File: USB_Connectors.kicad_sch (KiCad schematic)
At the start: 109 parts, among them J1 USB_C_Receptacle, J2 USB_C_Receptacle, J3 USB_C_Receptacle_USB2.0_16P, Q1 60/100V, Q2 60/100V, Q3 60/100V, Q4 60/100V, Q5 2N7002K, Q6 2N7002K, Q7 60/100V, Q8 2N7002K, Q9 60/100V, U2 RAA489400, U3 RAA489400, U4 RAA489400

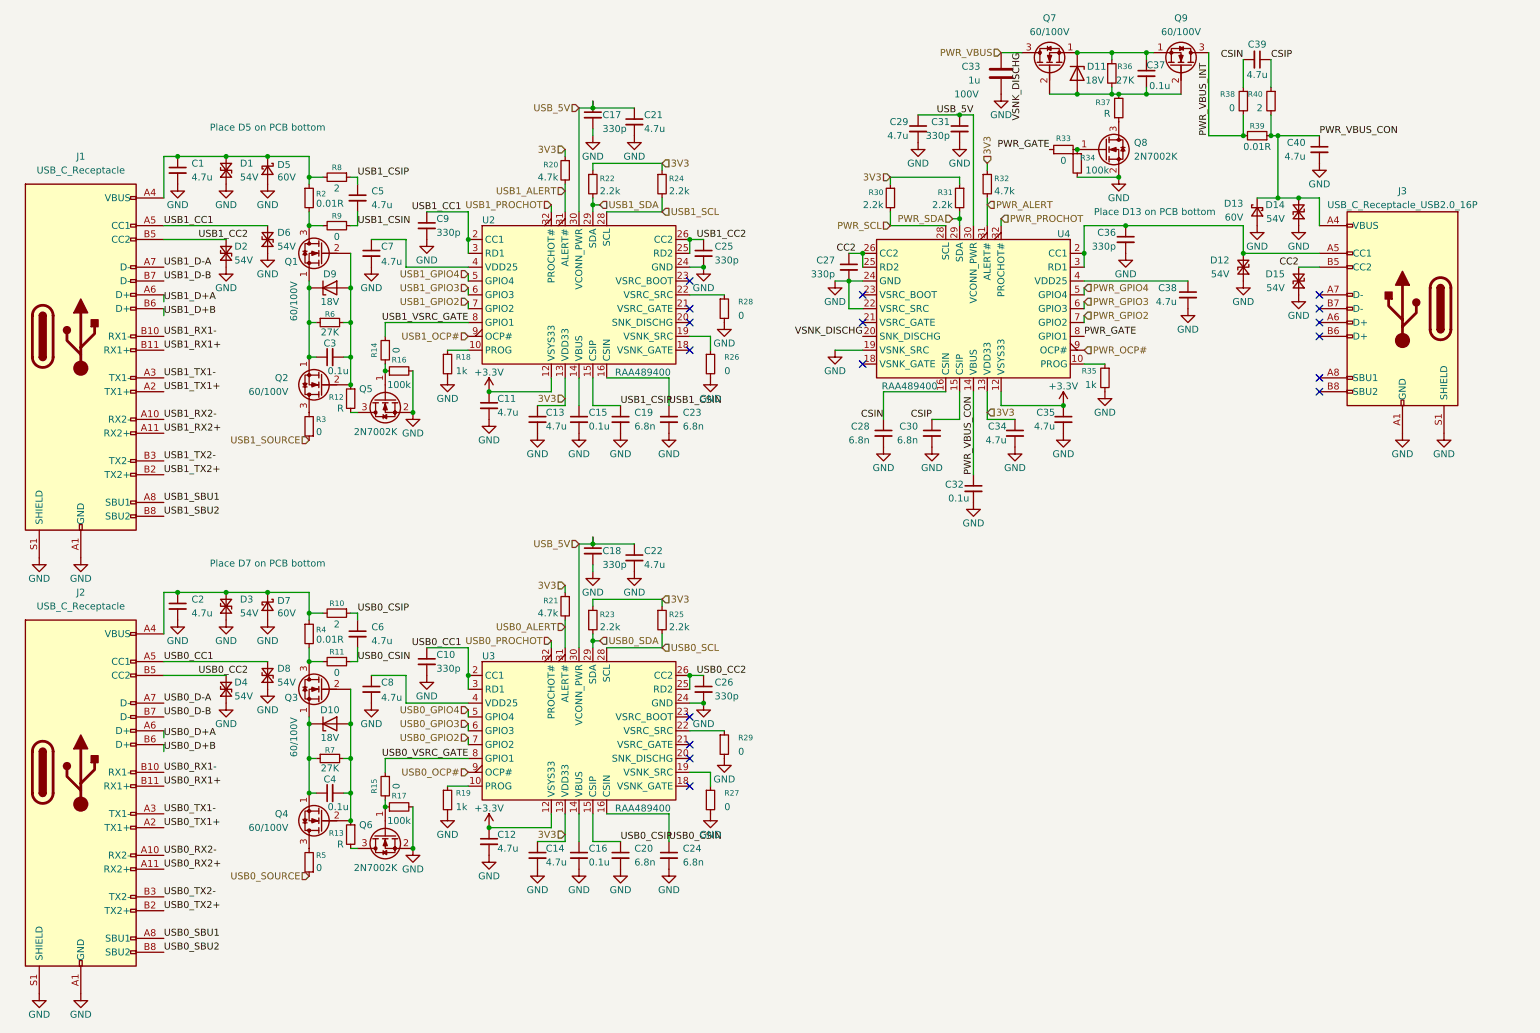
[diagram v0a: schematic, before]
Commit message: USB superspeed muxes
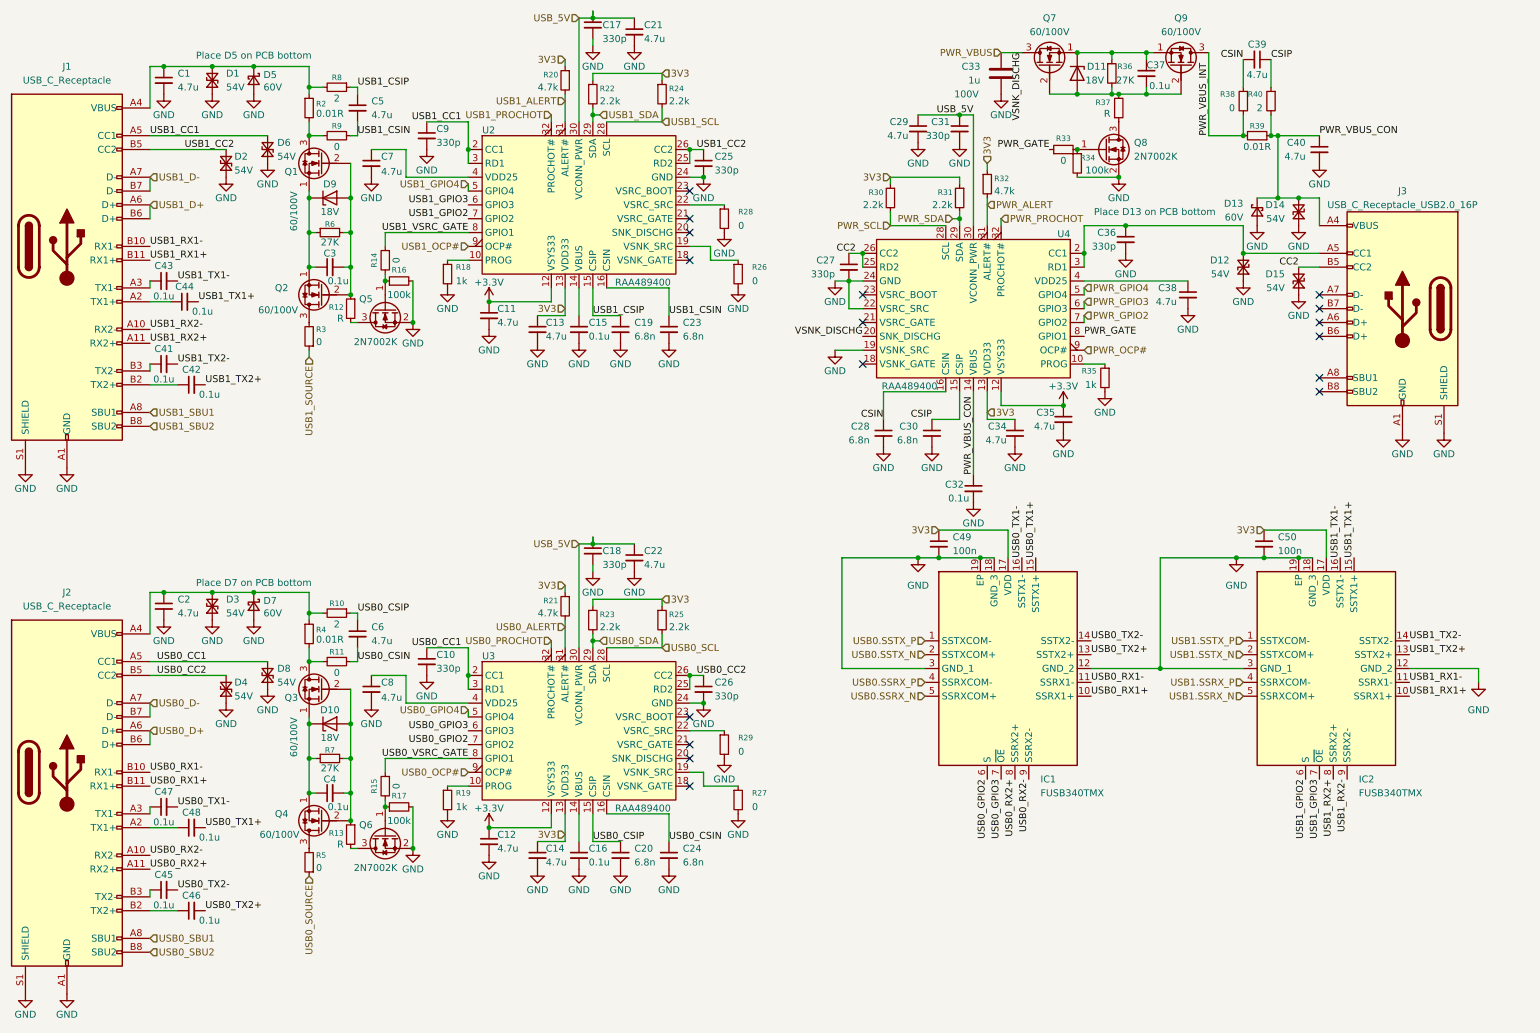
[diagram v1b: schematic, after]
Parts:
- added C41, C42, C43, C44, C45, C46, C47, C48: 0.1u, symbol Device:C_Small
- added C49, C50: 100n, symbol Device:C_Small
- added IC1, IC2: FUSB340TMX, onsemi:FUSB340TMX, symbol onsemi:FUSB340TMX
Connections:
- net USB0_D+B is gone; now on net USB0_D+: J2.B6 (D+)
- net USB0_D-B is gone; now on net USB0_D-: J2.B7 (D-)
- net USB1_D+B is gone; now on net USB1_D+: J1.B6 (D+)
- net USB1_D-B is gone; now on net USB1_D-: J1.B7 (D-)
- net 3V3: now also C49.1, C50.1, IC1.17 (VDD), IC2.17 (VDD)
- net GND: now also C49.2, C50.2, IC1.12 (GND_2), IC1.18 (GND_3), IC1.19 (EP), IC1.3 (GND_1), IC2.12 (GND_2), IC2.18 (GND_3), IC2.19 (EP), IC2.3 (GND_1)
- net USB0_GPIO2: now also IC1.6 (S)
- net USB0_GPIO3: now also IC1.7 (~{OE})
- net USB0_RX1+: now also IC1.10 (SSRX1+)
- net USB0_RX1-: now also IC1.11 (SSRX1-)
- net USB0_RX2+: now also IC1.8 (SSRX2+)
- net USB0_RX2-: now also IC1.9 (SSRX2-)
- net USB0_TX1+: now also C48.2, IC1.15 (SSTX1+); no longer J2.A2 (TX1+)
- net USB0_TX1-: now also C47.2, IC1.16 (SSTX1-); no longer J2.A3 (TX1-)
- net USB0_TX2+: now also C46.2, IC1.13 (SSTX2+); no longer J2.B2 (TX2+)
- net USB0_TX2-: now also C45.2, IC1.14 (SSTX2-); no longer J2.B3 (TX2-)
- net USB1_GPIO2: now also IC2.6 (S)
- net USB1_GPIO3: now also IC2.7 (~{OE})
- net USB1_RX1+: now also IC2.10 (SSRX1+)
- net USB1_RX1-: now also IC2.11 (SSRX1-)
- net USB1_RX2+: now also IC2.8 (SSRX2+)
- net USB1_RX2-: now also IC2.9 (SSRX2-)
- net USB1_TX1+: now also C44.2, IC2.15 (SSTX1+); no longer J1.A2 (TX1+)
- net USB1_TX1-: now also C43.2, IC2.16 (SSTX1-); no longer J1.A3 (TX1-)
- net USB1_TX2+: now also C42.2, IC2.13 (SSTX2+); no longer J1.B2 (TX2+)
- net USB1_TX2-: now also C41.2, IC2.14 (SSTX2-); no longer J1.B3 (TX2-)
- net USB0_D+A renamed USB0_D+
- net USB0_D-A renamed USB0_D-
- net USB1_D+A renamed USB1_D+
- net USB1_D-A renamed USB1_D-
- new net: C42.1, J1.B2 (TX2+)
- new net: C48.1, J2.A2 (TX1+)
- new net: C47.1, J2.A3 (TX1-)
- new net: C46.1, J2.B2 (TX2+)
- new net: C45.1, J2.B3 (TX2-)
- new net: C43.1, J1.A3 (TX1-)
- new net: C44.1, J1.A2 (TX1+)
- new net: C41.1, J1.B3 (TX2-)
- new net USB0.SSRX_N: IC1.5 (SSRXCOM+)
- new net USB0.SSRX_P: IC1.4 (SSRXCOM-)
- new net USB0.SSTX_N: IC1.2 (SSTXCOM+)
- new net USB0.SSTX_P: IC1.1 (SSTXCOM-)
- new net USB1.SSRX_N: IC2.5 (SSRXCOM+)
- new net USB1.SSRX_P: IC2.4 (SSRXCOM-)
- new net USB1.SSTX_N: IC2.2 (SSTXCOM+)
- new net USB1.SSTX_P: IC2.1 (SSTXCOM-)
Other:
- moved on the sheet: C1, C11, C13, C15, C17, C19, C2, C21, C23, C25, C3, C5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

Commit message: changed USB connectors added superspeed ESD updated USB-PD I2C PROG resistors
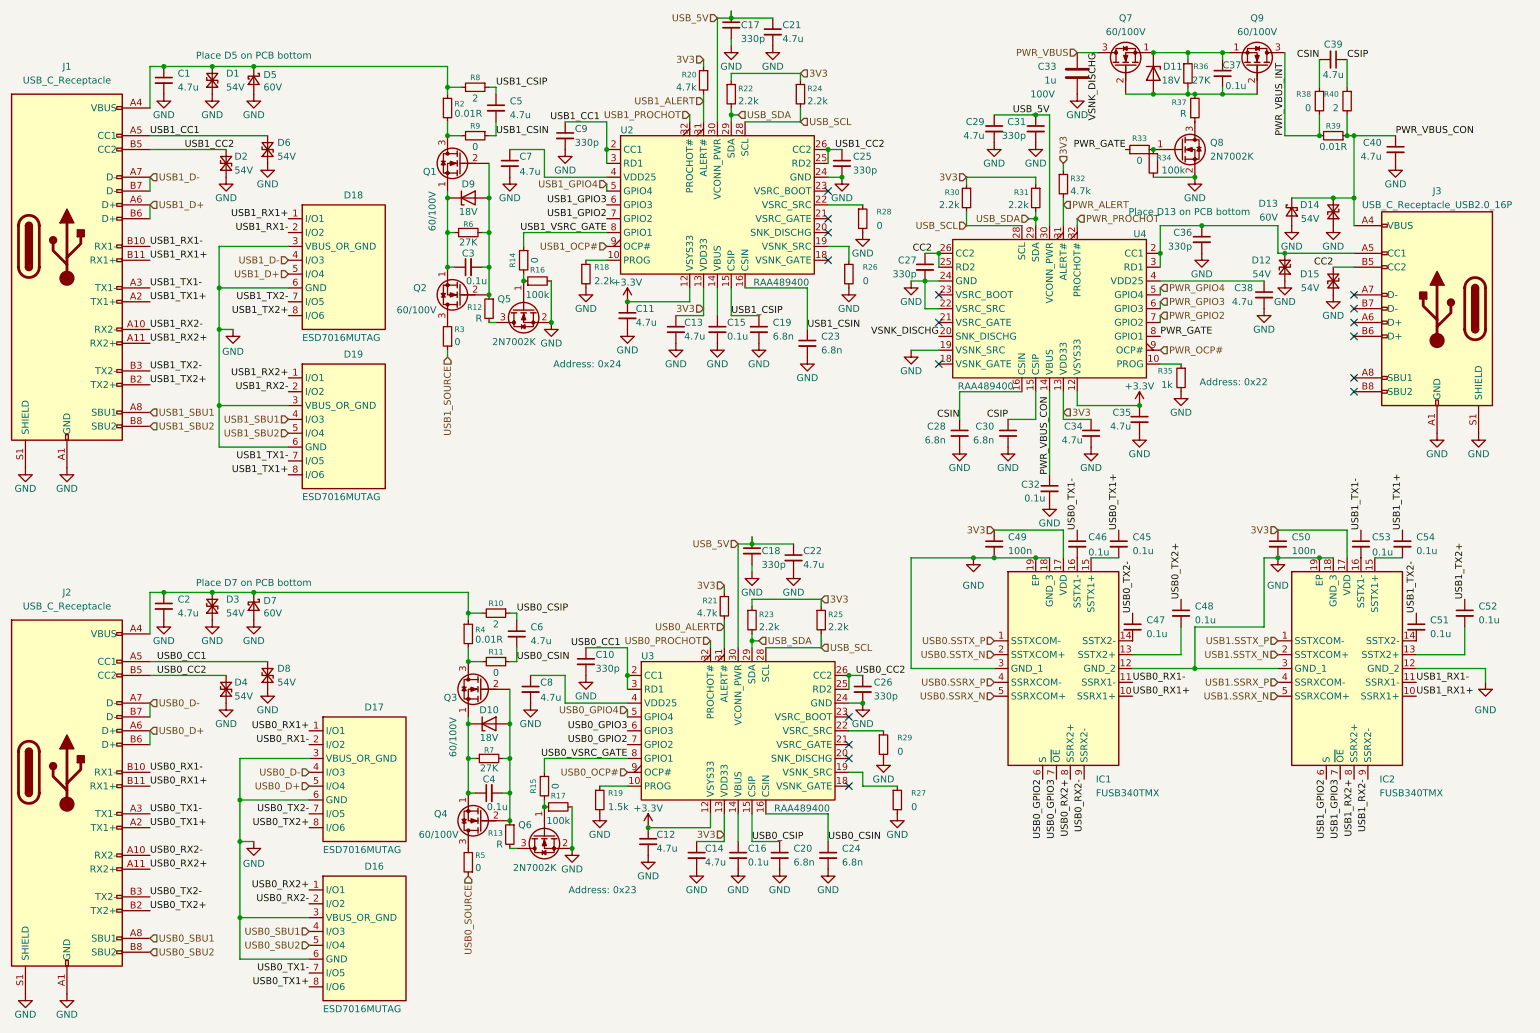
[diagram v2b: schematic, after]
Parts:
- removed C41, C42, C43, C44: 0.1u, symbol Device:C_Small
- added C51, C52, C53, C54: 0.1u, symbol Device:C_Small
- added D16, D17, D18, D19: ESD7016MUTAG, onsemi:ESD8006MUTAG, symbol onsemi:ESD7016MUTAG
- J1, J2: footprint (none) -> GCT:USB472503C
- J3: footprint Amphenol:GSB1C4621DS1HR -> GCT:USB472503C
- R18: value 1k -> 2.2k
- R19: value 1k -> 1.5k
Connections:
- net USB0_SCL is gone; now on net USB_SCL: R25.2, U3.28 (SCL)
- net USB0_SDA is gone; now on net USB_SDA: R23.2, U3.29 (SDA)
- net USB1_SCL is gone; now on net USB_SCL: R24.2, U2.28 (SCL)
- net USB1_SDA is gone; now on net USB_SDA: R22.2, U2.29 (SDA)
- net GND: now also D16.3 (VBUS_OR_GND), D16.6 (GND), D17.3 (VBUS_OR_GND), D17.6 (GND), D18.3 (VBUS_OR_GND), D18.6 (GND), D19.3 (VBUS_OR_GND), D19.6 (GND)
- net USB0_D+: now also D17.5 (I/O4)
- net USB0_D-: now also D17.4 (I/O3)
- net USB0_RX1+: now also D17.1 (I/O1)
- net USB0_RX1-: now also D17.2 (I/O2)
- net USB0_RX2+: now also D16.1 (I/O1)
- net USB0_RX2-: now also D16.2 (I/O2)
- net USB0_SBU1: now also D16.4 (I/O3)
- net USB0_SBU2: now also D16.5 (I/O4)
- net USB0_TX1+: now also C45.1, J2.A2 (TX1+), D16.8 (I/O6); no longer C48.2, IC1.15 (SSTX1+)
- net USB0_TX1-: now also C46.1, J2.A3 (TX1-), D16.7 (I/O5); no longer C47.2, IC1.16 (SSTX1-)
- net USB0_TX2+: now also C48.1, J2.B2 (TX2+), D17.8 (I/O6); no longer C46.2, IC1.13 (SSTX2+)
- net USB0_TX2-: now also C47.1, J2.B3 (TX2-), D17.7 (I/O5); no longer C45.2, IC1.14 (SSTX2-)
- net USB1_D+: now also D18.5 (I/O4)
- net USB1_D-: now also D18.4 (I/O3)
- net USB1_RX1+: now also D18.1 (I/O1)
- net USB1_RX1-: now also D18.2 (I/O2)
- net USB1_RX2+: now also D19.1 (I/O1)
- net USB1_RX2-: now also D19.2 (I/O2)
- net USB1_SBU1: now also D19.4 (I/O3)
- net USB1_SBU2: now also D19.5 (I/O4)
- net USB1_TX1+: now also J1.A2 (TX1+), C54.1, D19.8 (I/O6); no longer IC2.15 (SSTX1+)
- net USB1_TX1-: now also J1.A3 (TX1-), C53.1, D19.7 (I/O5); no longer IC2.16 (SSTX1-)
- net USB1_TX2+: now also J1.B2 (TX2+), C52.1, D18.8 (I/O6); no longer IC2.13 (SSTX2+)
- net USB1_TX2-: now also J1.B3 (TX2-), C51.1, D18.7 (I/O5); no longer IC2.14 (SSTX2-)
- net PWR_SCL renamed USB_SCL
- net PWR_SDA renamed USB_SDA
- new net: C54.2, IC2.15 (SSTX1+)
- new net: C52.2, IC2.13 (SSTX2+)
- new net: C47.2, IC1.14 (SSTX2-)
- new net: C46.2, IC1.16 (SSTX1-)
- new net: C53.2, IC2.16 (SSTX1-)
- new net: C51.2, IC2.14 (SSTX2-)
- new net: C45.2, IC1.15 (SSTX1+)
- new net: C48.2, IC1.13 (SSTX2+)
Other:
- moved on the sheet: C10, C11, C12, C13, C14, C15, C16, C17, C18, C19, C20, C21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

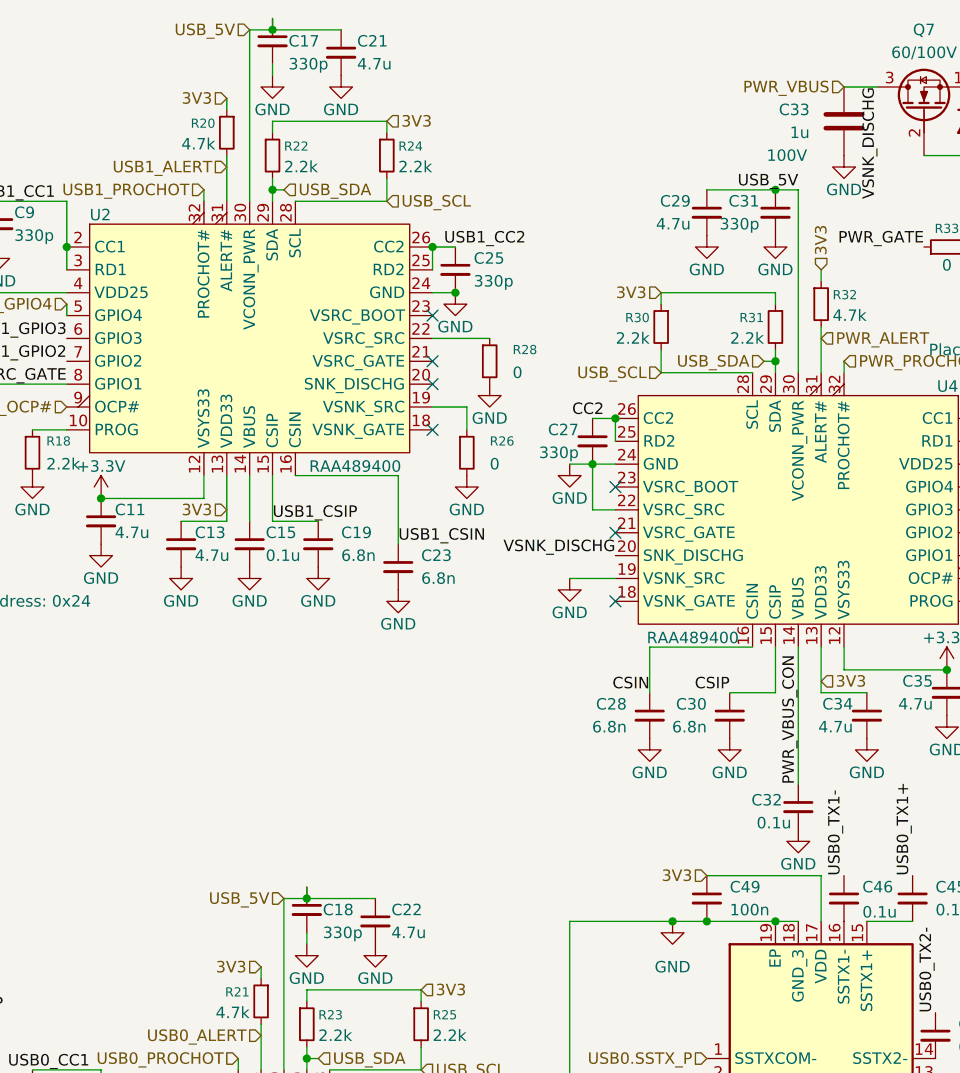
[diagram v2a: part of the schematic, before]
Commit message: USB 2.0 PHY
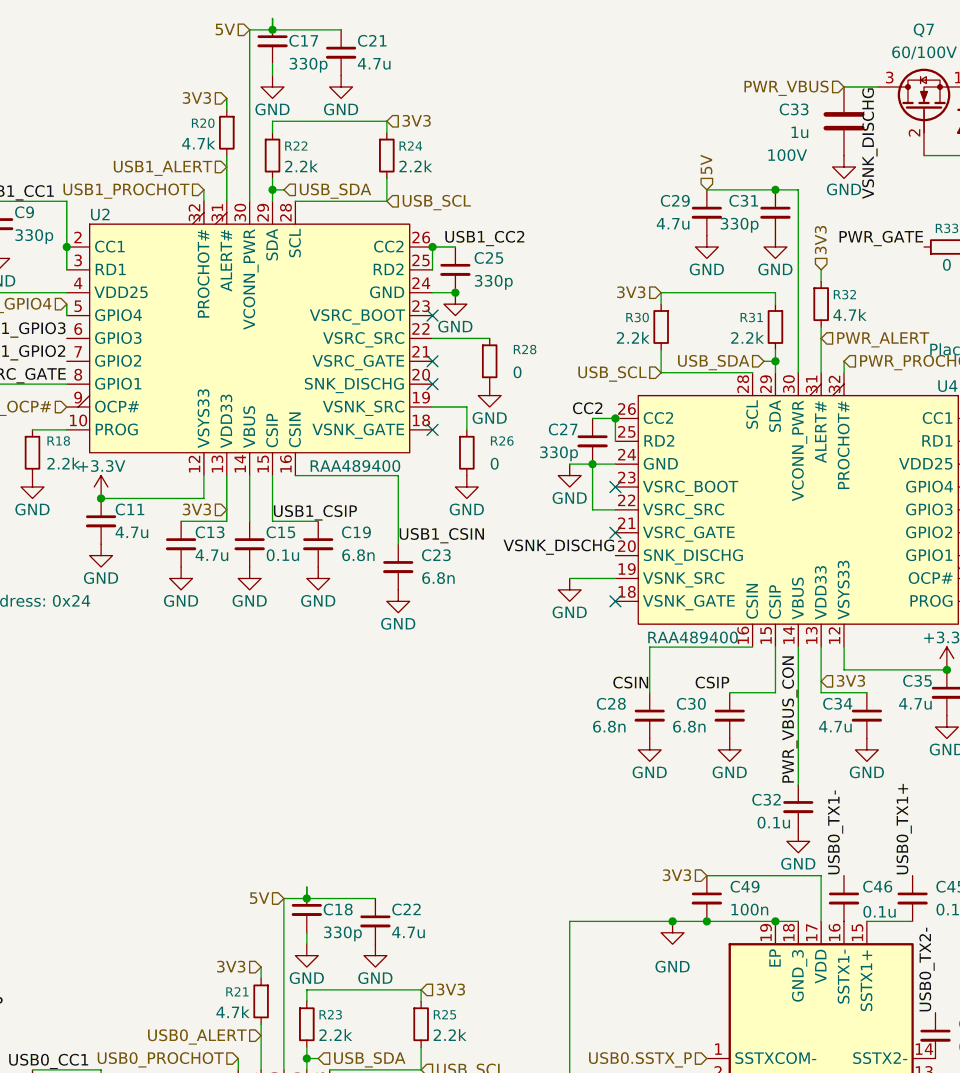
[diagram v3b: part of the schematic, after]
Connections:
- net USB_5V renamed 5V
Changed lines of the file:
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@@
-		)
-	)
-	(label "USB_5V"
-		(at 203.2 31.75 180)
-		(effects
-			(font
-				(size 1.27 1.27)
-			)
-			(justify right bottom)
 		)
 	)
@@
 		)
 	)
-	(hierarchical_label "USB_5V"
+	(hierarchical_label "5V"
 		(shape input)
 		(at 146.05 110.49 180)
@@
 		)
 	)
+	(hierarchical_label "5V"
+		(shape input)
+		(at 193.04 31.75 90)
+		(effects
+			(font
+				(size 1.27 1.27)
+			)
+			(justify left)
+		)
+	)
 	(hierarchical_label "USB0.SSRX_P"
 		(shape input)
@@
 		)
 	)
-	(hierarchical_label "USB_5V"
+	(hierarchical_label "5V"
 		(shape input)
 		(at 142.24 13.97 180)
